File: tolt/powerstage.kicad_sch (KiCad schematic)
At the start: 63 parts, among them Q1 NMOS, Q10 NMOS, Q11 NMOS, Q12 NMOS, Q13 NMOS, Q14 NMOS, Q15 NMOS, Q16 NMOS, Q17 NMOS, Q18 NMOS, Q2 NMOS, Q3 NMOS, Q4 NMOS, Q5 NMOS, Q6 NMOS, Q7 NMOS, Q8 NMOS, Q9 NMOS

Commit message: modified:   tolt/inter.kicad_sch 	modified:   tolt/powerstage.kicad_sch
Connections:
- net sens_a+: now reaches Q4.3 (S), Q5.3 (S), Q6.3 (S), R12.1, R13.1, R25.1
- net sens_c+: now reaches Q16.3 (S), Q17.3 (S), Q18.3 (S), R30.1, R31.1, R32.1
- net sens_b+: now reaches Q10.3 (S), Q11.3 (S), Q12.3 (S), R20.1, R21.1, R22.1
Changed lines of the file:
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@@
+	)
+	(junction
+		(at 225.298 79.756)
+		(diameter 0)
+		(color 0 0 0 0)
 	)
 	(junction
@@
 	)
 	(junction
+		(at 159.004 78.232)
+		(diameter 0)
+		(color 0 0 0 0)
+	)
+	(junction
+		(at 80.518 74.676)
+		(diameter 0)
+		(color 0 0 0 0)
+	)
+	(junction
 		(at 224.028 39.878)
 		(diameter 0)
@@
 	)
 	(junction
+		(at 63.754 74.676)
+		(diameter 0)
+		(color 0 0 0 0)
+	)
+	(junction
 		(at 137.922 62.484)
 		(diameter 0)
@@
 	)
 	(junction
+		(at 46.99 74.676)
+		(diameter 0)
+		(color 0 0 0 0)
+	)
+	(junction
+		(at 142.24 78.232)
+		(diameter 0)
+		(color 0 0 0 0)
+	)
+	(junction
 		(at 126.238 53.34)
 		(diameter 0)
@@
 	)
 	(junction
+		(at 175.768 78.232)
+		(diameter 0)
+		(color 0 0 0 0)
+	)
+	(junction
 		(at 30.988 49.784)
 		(diameter 0)
@@
 	)
 	(junction
+		(at 242.062 79.756)
+		(diameter 0)
+		(color 0 0 0 0)
+	)
+	(junction
 		(at 242.062 72.136)
 		(diameter 0)
@@
 	)
 	(junction
+		(at 258.826 79.756)
+		(diameter 0)
+		(color 0 0 0 0)
+	)
+	(junction
 		(at 137.922 41.148)
 		(diameter 0)
@@
 	(wire
 		(pts
+			(xy 225.298 79.756) (xy 242.062 79.756)
+		)
+		(stroke
+			(width 0)
+			(type default)
+		)
+	)
+	(wire
+		(pts
 			(xy 140.97 59.69) (xy 167.64 59.69)
 		)
@@
 	(wire
 		(pts
+			(xy 242.062 79.756) (xy 258.826 79.756)
+		)
+		(stroke
+			(width 0)
+			(type default)
+		)
+	)
+	(wire
+		(pts
 			(xy 63.754 32.766) (xy 46.99 32.766)
 		)
@@
 	(wire
 		(pts
+			(xy 80.518 74.676) (xy 63.754 74.676)
+		)
+		(stroke
+			(width 0)
+			(type default)
+		)
+	)
+	(wire
+		(pts
 			(xy 225.298 59.69) (xy 242.062 59.69)
 		)
@@
 	(wire
 		(pts
+			(xy 175.768 78.232) (xy 159.004 78.232)
+		)
+		(stroke
+			(width 0)
+			(type default)
+		)
+	)
+	(wire
+		(pts
 			(xy 126.238 34.798) (xy 126.238 38.354)
 		)
@@
 	(wire
 		(pts
+			(xy 63.754 74.676) (xy 46.99 74.676)
+		)
+		(stroke
+			(width 0)
+			(type default)
+		)
+	)
+	(wire
+		(pts
 			(xy 242.062 59.69) (xy 242.062 61.976)
 		)
@@
 		(pts
 			(xy 140.97 29.21) (xy 133.858 29.21)
+		)
+		(stroke
+			(width 0)
+			(type default)
+		)
+	)
+	(wire
+		(pts
+			(xy 159.004 78.232) (xy 142.24 78.232)
 		)
 		(stroke
@@
 		)
 	)
+	(hierarchical_label "sens_b+"
+		(shape input)
+		(at 175.768 70.612 0)
+		(effects
+			(font
+				(size 1.27 1.27)
+			)
+			(justify left)
+		)
+	)
+	(hierarchical_label "sens_a+"
+		(shape input)
+		(at 80.518 67.056 0)
+		(effects
+			(font
+				(size 1.27 1.27)
+			)
+			(justify left)
+		)
+	)
 	(hierarchical_label "G_H_B"
 		(shape bidirectional)
@@
 		)
 	)
+	(hierarchical_label "sens_c-"
+		(shape input)
+		(at 258.826 79.756 0)
+		(effects
+			(font
+				(size 1.27 1.27)
+			)
+			(justify left)
+		)
+	)
 	(hierarchical_label "G_L_C"
 		(shape bidirectional)
@@
 		)
 	)
+	(hierarchical_label "sens_c+"
+		(shape input)
+		(at 258.826 72.136 0)
+		(effects
+			(font
+				(size 1.27 1.27)
+			)
+			(justify left)
+		)
+	)
+	(hierarchical_label "sens_a-"
+		(shape input)
+		(at 80.518 74.676 0)
+		(effects
+			(font
+				(size 1.27 1.27)
+			)
+			(justify left)
+		)
+	)
 	(hierarchical_label "G_L_A"
 		(shape bidirectional)
@@
 		(effects
 			(font
+				(size 1.27 1.27)
+			)
+			(justify left)
+		)
+	)
+	(hierarchical_label "sens_b-"
+		(shape input)
+		(at 175.768 78.232 0)
+		(effects
+			(font

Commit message: modified:   tolt/inter.kicad_sch 	modified:   tolt/powerstage.kicad_sch 	modified:   tolt/stm32.kicad_sch 	modified:   tolt/tolt.kicad_sch
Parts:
- added C58, C59, C60: 2.2uf, Capacitor_SMD:C_0603_1608Metric, symbol Device:C
- added R58, R59, R60: 10k_NTC, Resistor_SMD:R_0603_1608Metric_Pad0.98x0.95mm_HandSolder, symbol Device:R
- added R61, R62, R63: 10k, Resistor_SMD:R_0603_1608Metric, symbol Device:R
- R12, R13, R20, R21, R22, R25, R30, R31, R32: value R -> 0.3mr
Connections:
- net GNDPWR: no longer R25.2
- net sens_a+: no longer R25.1
- new net GND: C58.2, C59.2, C60.2, R61.2, R62.2, R63.2
- new net TEMP: C58.1, R58.2, R61.1
- new net TEMP1: C59.1, R59.2, R62.1
- new net TEMP2: C60.1, R60.2, R63.1
- new net VCC: R58.1, R59.1, R60.1
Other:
- note added: "0.3mr with 20gain 0.1mr with 50gain"
- note added: "temp sensing"
- moved on the sheet: R25

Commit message: Converters
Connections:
- net GNDPWR: no longer R20.2, R30.2
- net sens_b+: no longer R20.1
- net sens_c+: no longer R30.1
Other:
- moved on the sheet: R20, R30

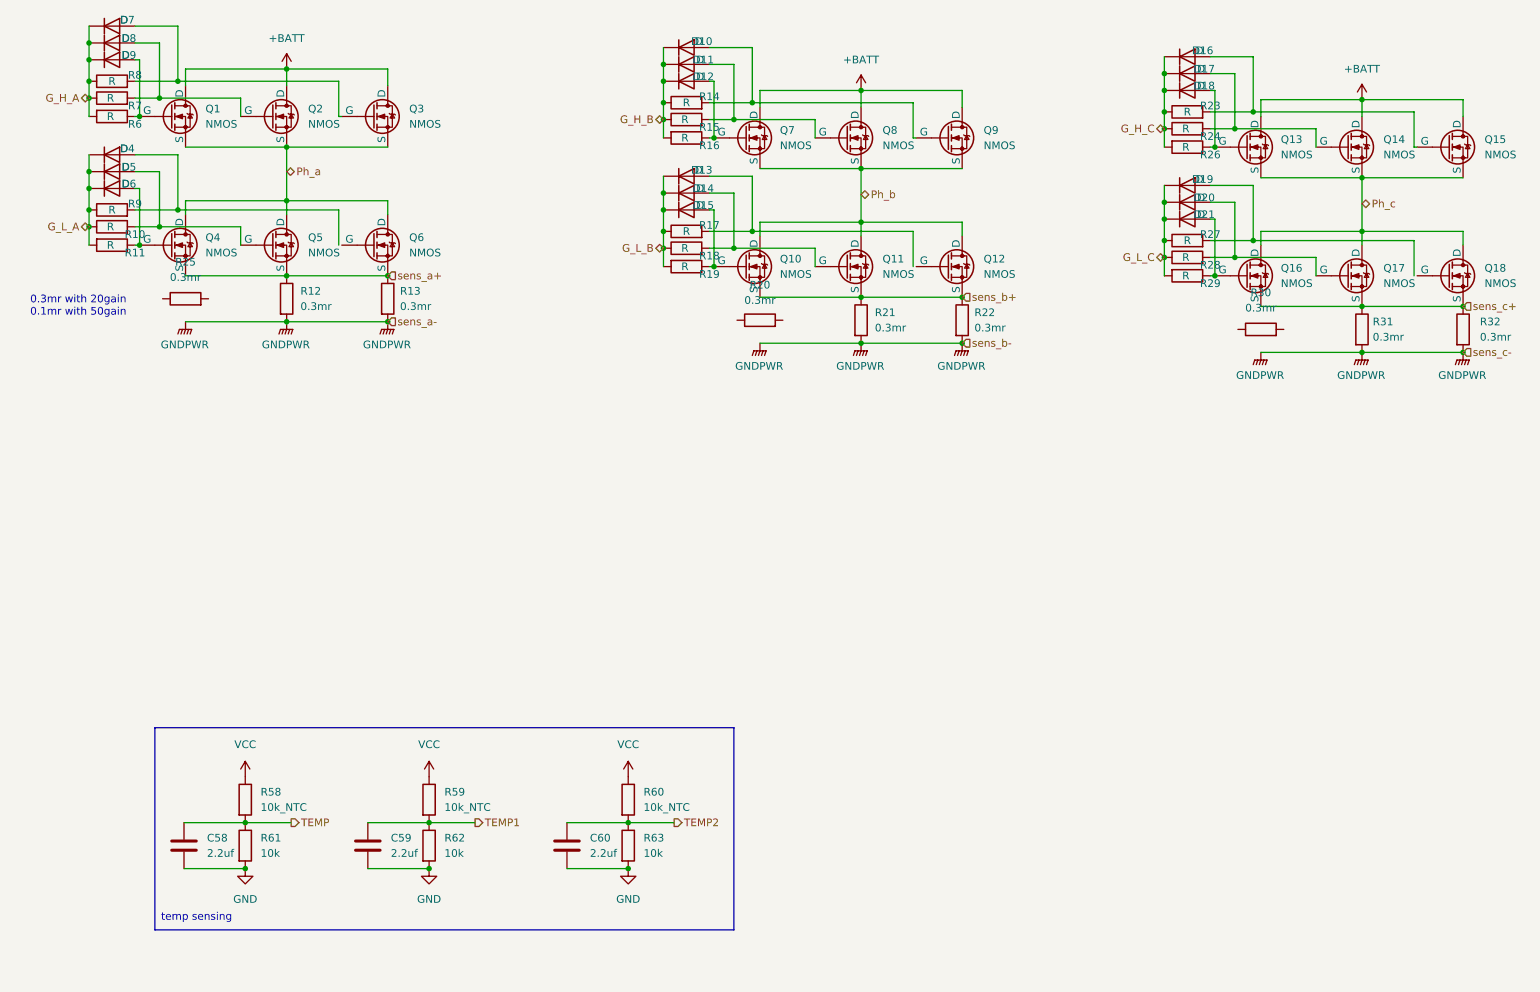
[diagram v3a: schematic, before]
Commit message: modified:   tolt/auxl.kicad_sch 	modified:   tolt/converters.kicad_sch 	modified:   tolt/powerstage.kicad_sch 	modified:   tolt/stm32.kicad_sch 	modified:   tolt/tolt.kicad_pcb 	modified:   tolt/tolt.kicad_pro 	modified:   tolt/tolt.kicad_sch 	SOP120P1500X235-17N.step 	tolt/Library.pretty/HDSOP-16-2.kicad_mod 	tolt/Library.pretty/R5930.kicad_mod 	tolt/conn.kicad_sch
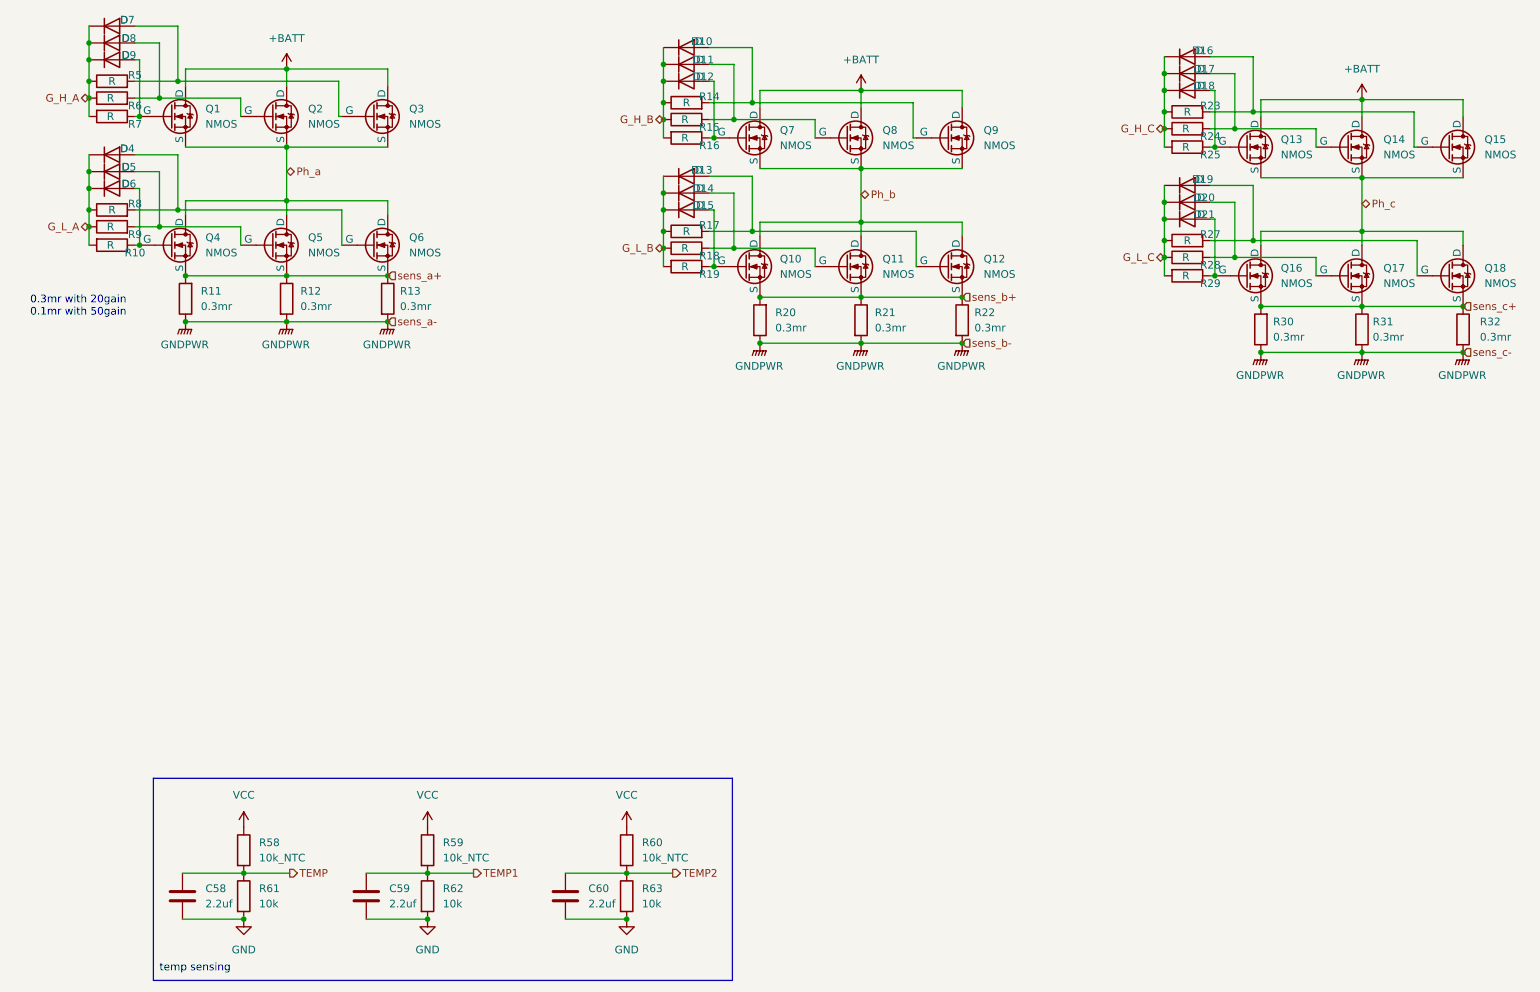
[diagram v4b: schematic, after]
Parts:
- Q1, Q10, Q11, Q12, Q13, Q14, Q15, Q16, Q17, Q18, Q2, Q3, Q4, Q5, Q6, Q7, Q8, Q9: footprint (none) -> Library:HDSOP-16-2
- R11: renamed from R25; footprint (none) -> Library:R5930
- R12, R13, R20, R21, R22, R30, R31, R32: footprint (none) -> Library:R5930
- renumbered R11 to R10, R26 to R25, R8 to R5, R7 to R6, R6 to R7, R9 to R8, R10 to R9
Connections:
- net GNDPWR: now also R11.1, R20.1, R30.1
- net sens_a+: now also R11.2
- net sens_b+: now also R20.2
- net sens_c+: now also R30.2
- net at D19.2 (A), R27.2: now also Q18.2 (G)
- net at D13.2 (A), R17.2: now also Q12.2 (G)
- net at D4.2 (A), R8.2: now also Q6.2 (G)
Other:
- moved on the sheet: C58, C59, C60, R11, R20, R30, R58, R59, R60, R61, R62, R63

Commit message: footprints
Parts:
- R10, R14, R15, R16, R17, R18, R19, R23, R24, R25, R27, R28, R29, R5, R6, R7, R8, R9: footprint (none) -> Resistor_SMD:R_0603_1608Metric
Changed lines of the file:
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@@
 			)
 		)
-		(property "Footprint" ""
+		(property "Footprint" "Resistor_SMD:R_0603_1608Metric"
 			(at 34.798 39.37 90)
 			(effects
@@
 			)
 		)
-		(property "Footprint" ""
+		(property "Footprint" "Resistor_SMD:R_0603_1608Metric"
 			(at 213.106 41.656 90)
 			(effects
@@
 			)
 		)
-		(property "Footprint" ""
+		(property "Footprint" "Resistor_SMD:R_0603_1608Metric"
 			(at 213.106 65.786 90)
 			(effects
@@
 			)
 		)
-		(property "Footprint" ""
+		(property "Footprint" "Resistor_SMD:R_0603_1608Metric"
 			(at 130.048 64.262 90)
 			(effects
@@
 			)
 		)
-		(property "Footprint" ""
+		(property "Footprint" "Resistor_SMD:R_0603_1608Metric"
 			(at 130.048 63.754 90)
 			(effects
@@
 			)
 		)
-		(property "Footprint" ""
+		(property "Footprint" "Resistor_SMD:R_0603_1608Metric"
 			(at 213.106 65.278 90)
 			(effects
@@
 			)
 		)
-		(property "Footprint" ""
+		(property "Footprint" "Resistor_SMD:R_0603_1608Metric"
 			(at 130.048 61.468 90)
 			(effects
@@
 			)
 		)
-		(property "Footprint" ""
+		(property "Footprint" "Resistor_SMD:R_0603_1608Metric"
 			(at 213.106 43.942 90)
 			(effects
@@
 			)
 		)
-		(property "Footprint" ""
+		(property "Footprint" "Resistor_SMD:R_0603_1608Metric"
 			(at 34.798 60.198 90)
 			(effects
@@
 			)
 		)
-		(property "Footprint" ""
+		(property "Footprint" "Resistor_SMD:R_0603_1608Metric"
 			(at 34.798 38.862 90)
 			(effects
@@
 			)
 		)
-		(property "Footprint" ""
+		(property "Footprint" "Resistor_SMD:R_0603_1608Metric"
 			(at 34.798 57.912 90)
 			(effects
@@
 			)
 		)
-		(property "Footprint" ""
+		(property "Footprint" "Resistor_SMD:R_0603_1608Metric"
 			(at 34.798 60.706 90)
 			(effects
@@
 			)
 		)
-		(property "Footprint" ""
+		(property "Footprint" "Resistor_SMD:R_0603_1608Metric"
 			(at 34.798 36.576 90)
 			(effects
@@
 			)
 		)
-		(property "Footprint" ""
+		(property "Footprint" "Resistor_SMD:R_0603_1608Metric"
 			(at 213.106 62.992 90)
 			(effects
@@
 			)
 		)
-		(property "Footprint" ""
+		(property "Footprint" "Resistor_SMD:R_0603_1608Metric"
 			(at 130.048 42.418 90)
 			(effects
@@
 			)
 		)
-		(property "Footprint" ""
+		(property "Footprint" "Resistor_SMD:R_0603_1608Metric"
 			(at 213.106 44.45 90)
 			(effects
@@
 			)
 		)
-		(property "Footprint" ""
+		(property "Footprint" "Resistor_SMD:R_0603_1608Metric"
 			(at 130.048 42.926 90)
 			(effects
@@
 			)
 		)
-		(property "Footprint" ""
+		(property "Footprint" "Resistor_SMD:R_0603_1608Metric"
 			(at 130.048 40.132 90)
 			(effects
